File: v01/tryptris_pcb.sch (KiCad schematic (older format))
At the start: 131 parts, among them J1 USB_C_Receptacle_USB2.0, J2 I2C-L, J3 I2C-R, SW1 Reset, U1 ATmega32U4-AU, U2 MCP23017_SO, Y1 16Mhz

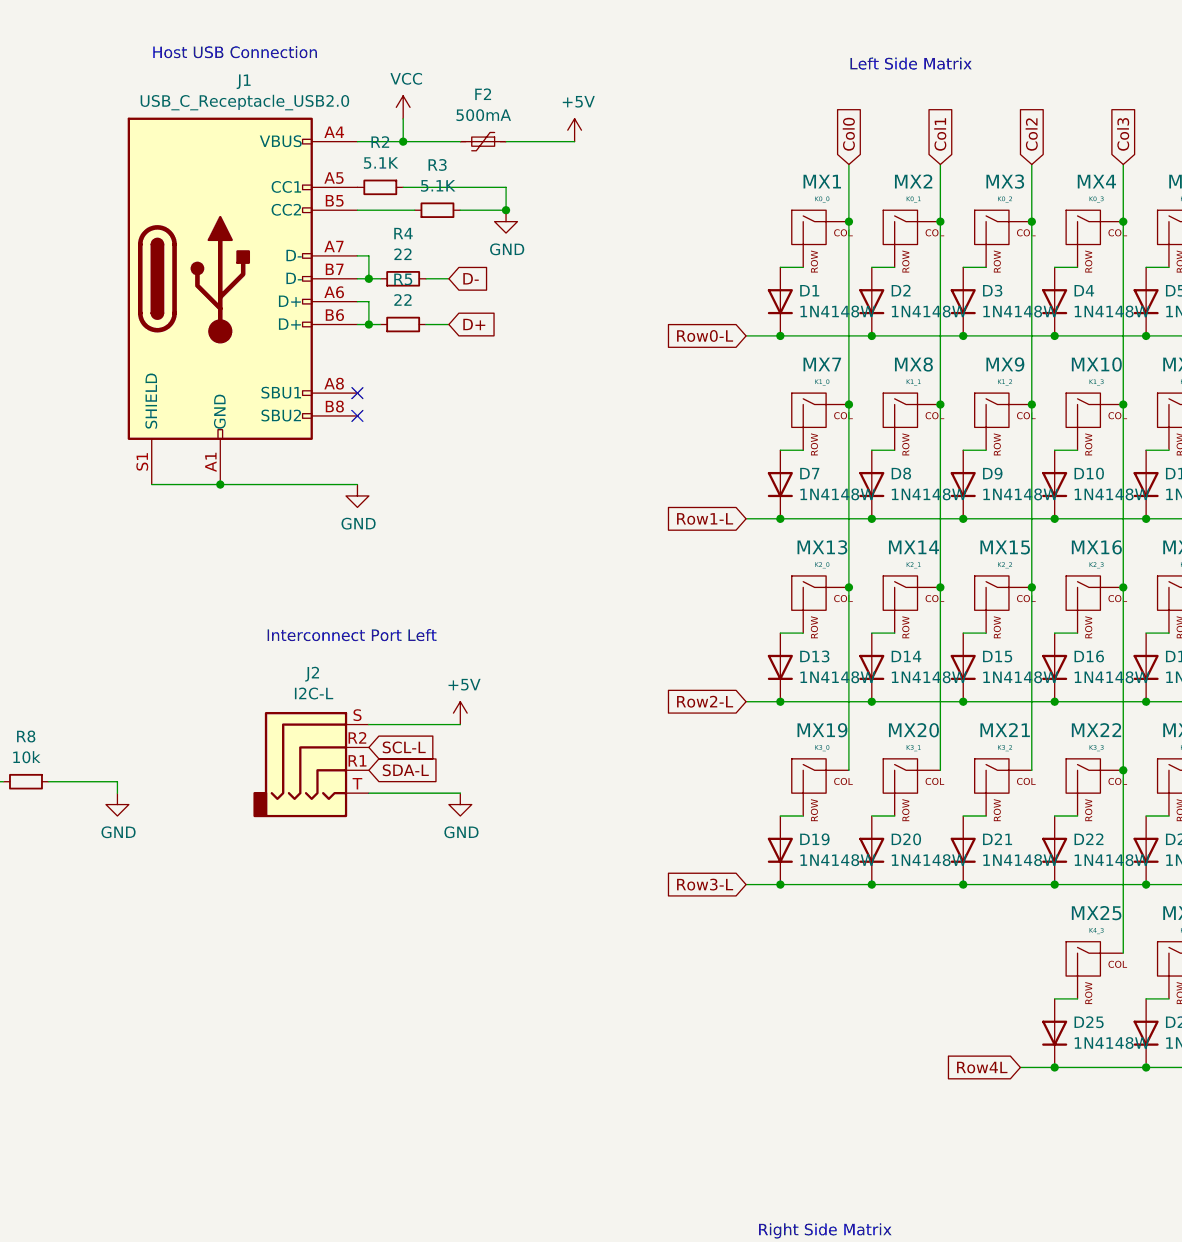
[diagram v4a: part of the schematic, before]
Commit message: Made progress on the left side routing.
I am going to put the components on the bottom (except diodes), and
ports on the top so that the board can be lower to the table.

A bunch of routing for the left side is done after a few different
attempts.
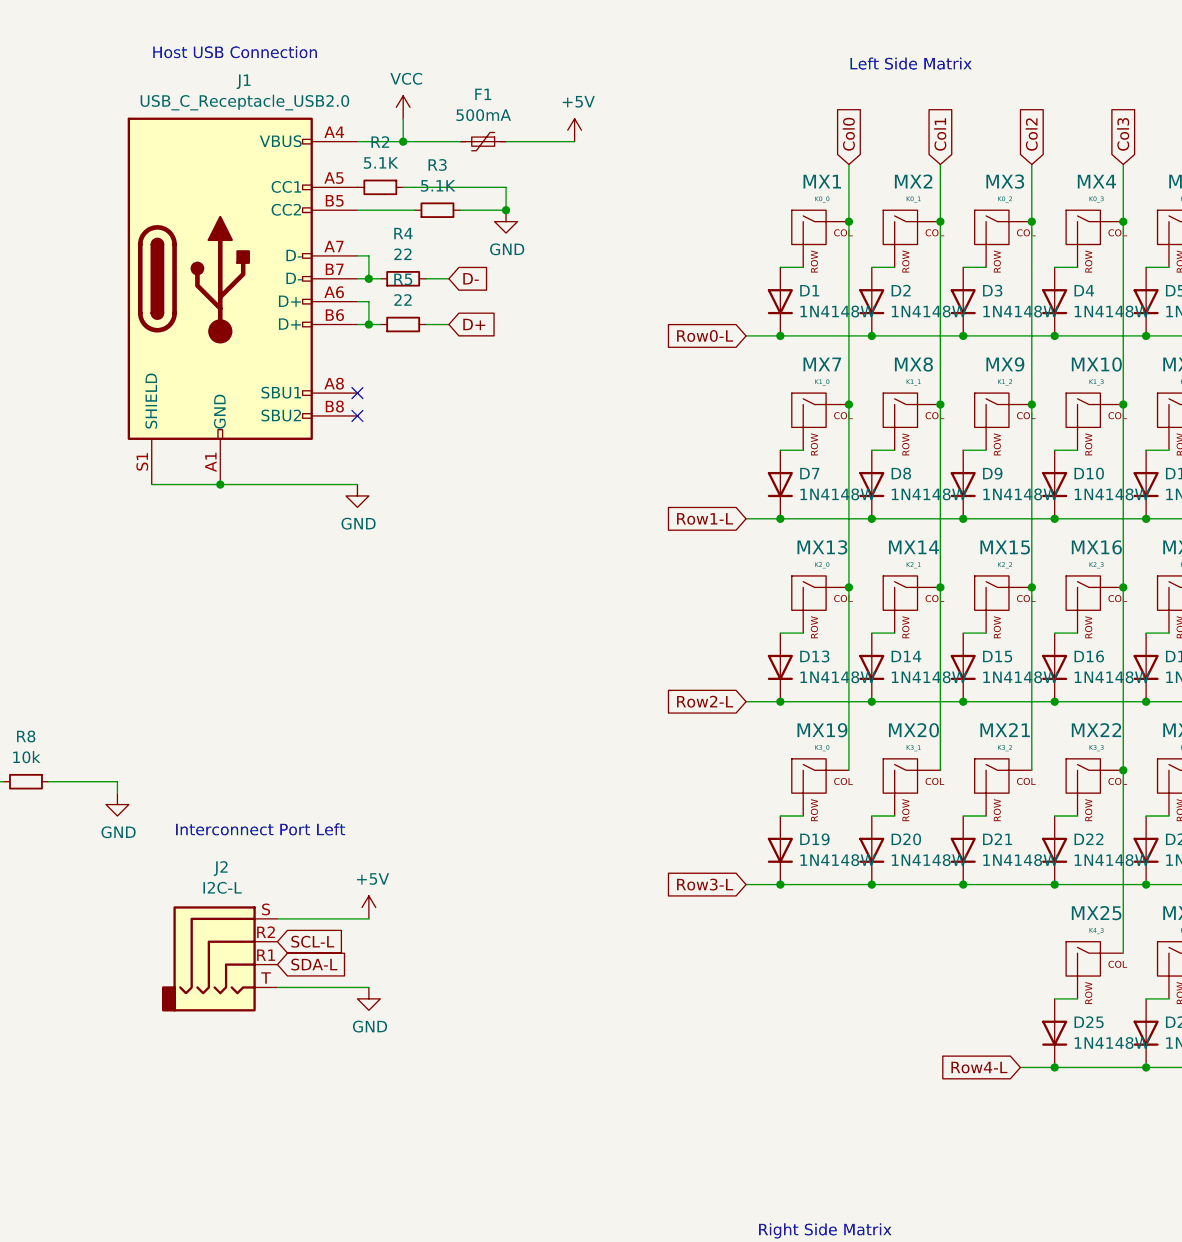
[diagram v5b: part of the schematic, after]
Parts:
- renumbered F2 to F1
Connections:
- net Row4L is gone; now on net Row4-L: D25.1 (K), D26.1 (K), D27.1 (K)
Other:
- moved on the sheet: J2
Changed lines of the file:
@@
 Row3-L
 Text GLabel 8600 5100 0    50   Input ~ 0
-Row4L
+Row4-L
 Text GLabel 7850 1150 1    50   Input ~ 0
 Col0
@@
 Text Notes 4350 6300 0    50   ~ 0
 Interconnect port Right
-Text GLabel 5750 3700 2    50   Input ~ 0
+Text GLabel 5350 4550 2    50   Input ~ 0
 SCL-L
-Text GLabel 5750 3800 2    50   Input ~ 0
+Text GLabel 5350 4650 2    50   Input ~ 0
 SDA-L
-Text Notes 5300 3250 0    50   ~ 0
+Text Notes 4900 4100 0    50   ~ 0
 Interconnect Port Left
 $Comp
 L power:GND #PWR0117
 U 1 1 6172F5A1
-P 6150 3900
-F 0 "#PWR0117" H 6150 3650 50  0001 C CNN
-F 1 "GND" H 6155 3727 50  0000 C CNN
-F 2 "" H 6150 3900 50  0001 C CNN
-F 3 "" H 6150 3900 50  0001 C CNN
-	1    6150 3900
-	1    0    0    -1
-$EndComp
-Wire Wire Line
-	6150 3900 5750 3900
+P 5750 4750
+F 0 "#PWR0117" H 5750 4500 50  0001 C CNN
+F 1 "GND" H 5755 4577 50  0000 C CNN
+F 2 "" H 5750 4750 50  0001 C CNN
+F 3 "" H 5750 4750 50  0001 C CNN
+	1    5750 4750
+	1    0    0    -1
+$EndComp
+Wire Wire Line
+	5750 4750 5350 4750
 $Comp
 L power:GND #PWR0118
@@
 L power:+5V #PWR0122
 U 1 1 618ACD08
-P 6150 3600
-F 0 "#PWR0122" H 6150 3450 50  0001 C CNN
-F 1 "+5V" H 6165 3773 50  0000 C CNN
-F 2 "" H 6150 3600 50  0001 C CNN
-F 3 "" H 6150 3600 50  0001 C CNN
-	1    6150 3600
-	1    0    0    -1
-$EndComp
-Wire Wire Line
-	6150 3600 5750 3600
+P 5750 4450
+F 0 "#PWR0122" H 5750 4300 50  0001 C CNN
+F 1 "+5V" H 5765 4623 50  0000 C CNN
+F 2 "" H 5750 4450 50  0001 C CNN
+F 3 "" H 5750 4450 50  0001 C CNN
+	1    5750 4450
+	1    0    0    -1
+$EndComp
+Wire Wire Line
+	5750 4450 5350 4450
 Wire Wire Line
 	5700 7100 5550 7100
@@
 $EndComp
 $Comp
-L Device:Polyfuse_Small F2
+L Device:Polyfuse_Small F1
 U 1 1 61BE2113
 P 6250 1050
-F 0 "F2" V 6045 1050 50  0000 C CNN
+F 0 "F1" V 6045 1050 50  0000 C CNN
 F 1 "500mA" V 6136 1050 50  0000 C CNN
 F 2 "Fuse:Fuse_1206_3216Metric" H 6300 850 50  0001 L CNN
@@
 L Connector:AudioJack4 J2
 U 1 1 62111EC5
-P 5550 3700
-F 0 "J2" H 5507 4025 50  0000 C CNN
-F 1 "I2C-L" H 5507 3934 50  0000 C CNN
-F 2 "Connector_Audio:Jack_3.5mm_PJ320E_Horizontal" H 5550 3700 50  0001 C CNN
-F 3 "~" H 5550 3700 50  0001 C CNN
-	1    5550 3700
-	1    0    0    -1
-$EndComp
+P 5150 4550
+F 0 "J2" H 5107 4875 50  0000 C CNN
+F 1 "I2C-L" H 5107 4784 50  0000 C CNN
+F 2 "Connector_Audio:Jack_3.5mm_PJ320E_Horizontal" H 5150 4550 50  0001 C CNN
+F 3 "~" H 5150 4550 50  0001 C CNN
+	1    5150 4550
+	1    0    0    -1
+$EndComp

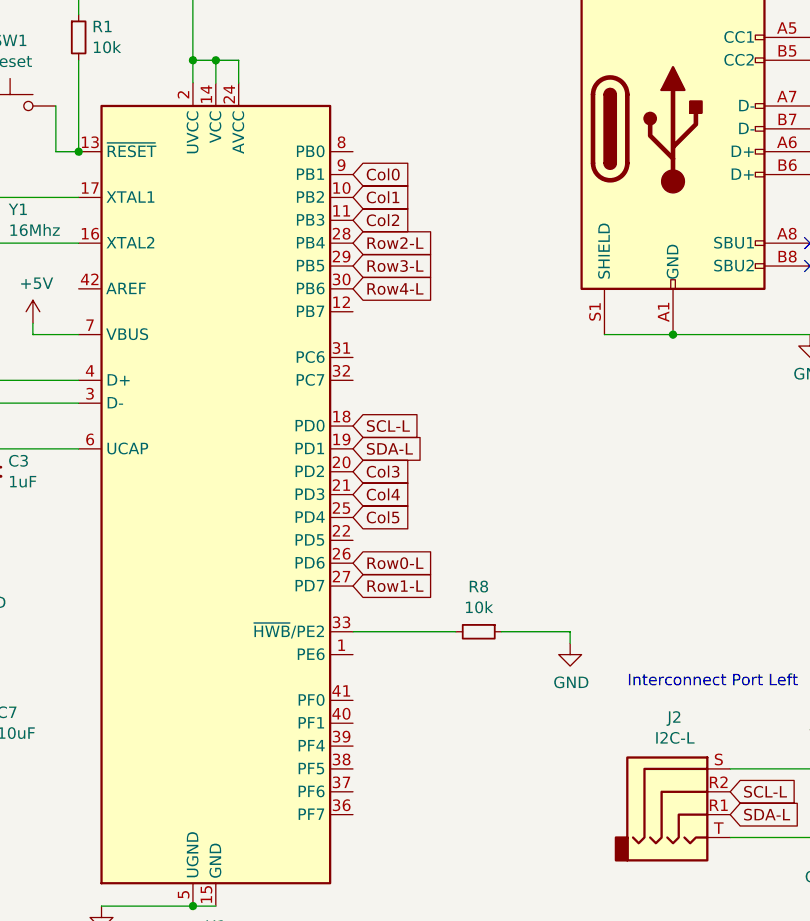
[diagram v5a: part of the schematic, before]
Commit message: Move components to a block outside the switch matrix
* Having the ports top mounted will let the board be lower profile.
* Having the components on top looks kind of cool too.
* Roughly routed the entire left sideci!
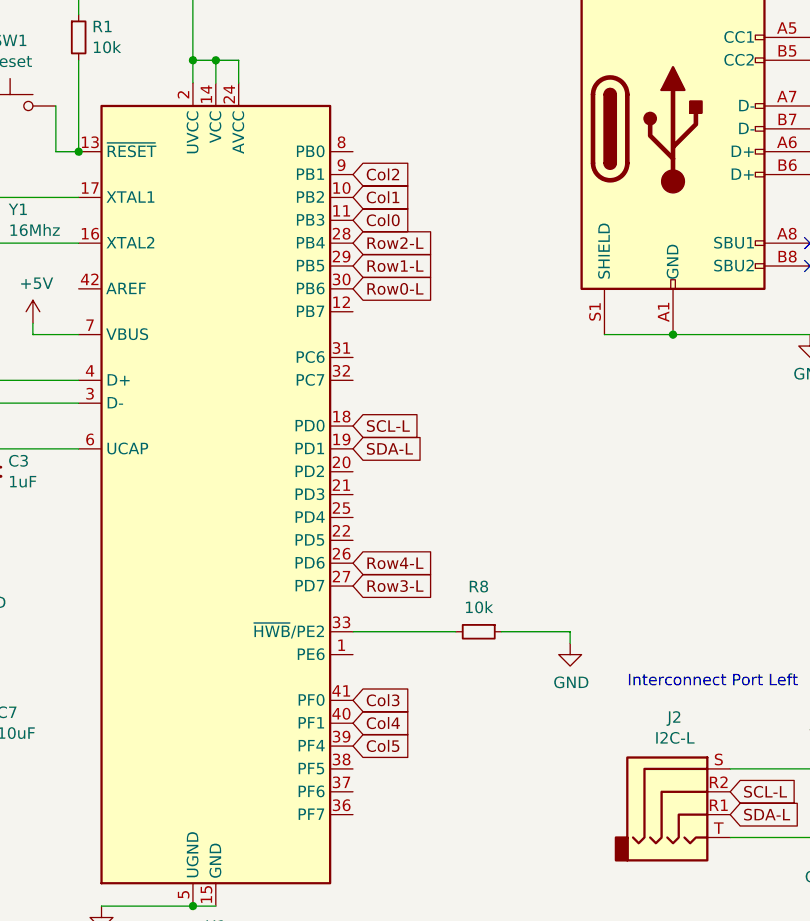
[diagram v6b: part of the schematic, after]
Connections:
- net Col0: now also U1.11 (PB3); no longer U1.9 (PB1)
- net Col2: now also U1.9 (PB1); no longer U1.11 (PB3)
- net Col3: now also U1.41 (PF0); no longer U1.20 (PD2)
- net Col4: now also U1.40 (PF1); no longer U1.21 (PD3)
- net Col5: now also U1.39 (PF4); no longer U1.25 (PD4)
- net Row0-L: now also U1.30 (PB6); no longer U1.26 (PD6)
- net Row1-L: now also U1.29 (PB5); no longer U1.27 (PD7)
- net Row3-L: now also U1.27 (PD7); no longer U1.29 (PB5)
- net Row4-L: now also U1.26 (PD6); no longer U1.30 (PB6)
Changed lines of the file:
@@
 	9050 3800 9050 4600
 Connection ~ 9050 3800
-Text GLabel 3700 3550 2    50   Input ~ 0
+Text GLabel 3700 2350 2    50   Input ~ 0
 Row0-L
-Text GLabel 3700 3650 2    50   Input ~ 0
+Text GLabel 3700 2250 2    50   Input ~ 0
 Row1-L
 Text GLabel 3700 2150 2    50   Input ~ 0
 Row2-L
-Text GLabel 3700 2250 2    50   Input ~ 0
+Text GLabel 3700 3650 2    50   Input ~ 0
 Row3-L
-Text GLabel 3700 2350 2    50   Input ~ 0
+Text GLabel 3700 3550 2    50   Input ~ 0
 Row4-L
-Text GLabel 3700 1850 2    50   Input ~ 0
+Text GLabel 3700 2050 2    50   Input ~ 0
 Col0
 Text GLabel 3700 1950 2    50   Input ~ 0
 Col1
-Text GLabel 3700 2050 2    50   Input ~ 0
+Text GLabel 3700 1850 2    50   Input ~ 0
 Col2
-Text GLabel 3700 3150 2    50   Input ~ 0
+Text GLabel 3700 4150 2    50   Input ~ 0
 Col3
-Text GLabel 3700 3250 2    50   Input ~ 0
+Text GLabel 3700 4250 2    50   Input ~ 0
 Col4
-Text GLabel 3700 3350 2    50   Input ~ 0
+Text GLabel 3700 4350 2    50   Input ~ 0
 Col5
 Text Notes 2800 6200 0    50   ~ 0
